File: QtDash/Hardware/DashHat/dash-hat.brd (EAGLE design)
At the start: 120.9 x 74.9 mm, 166 parts, among them IC1 LMV614, IC10 MAX9924, IC11 ZXTR2105FQ, IC2 MCP3X083008, IC3 MCP23017SS, IC4 LM358D, IC5 IL300, IC6 TSV912D, IC7 IL300, IC8 TSV912D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

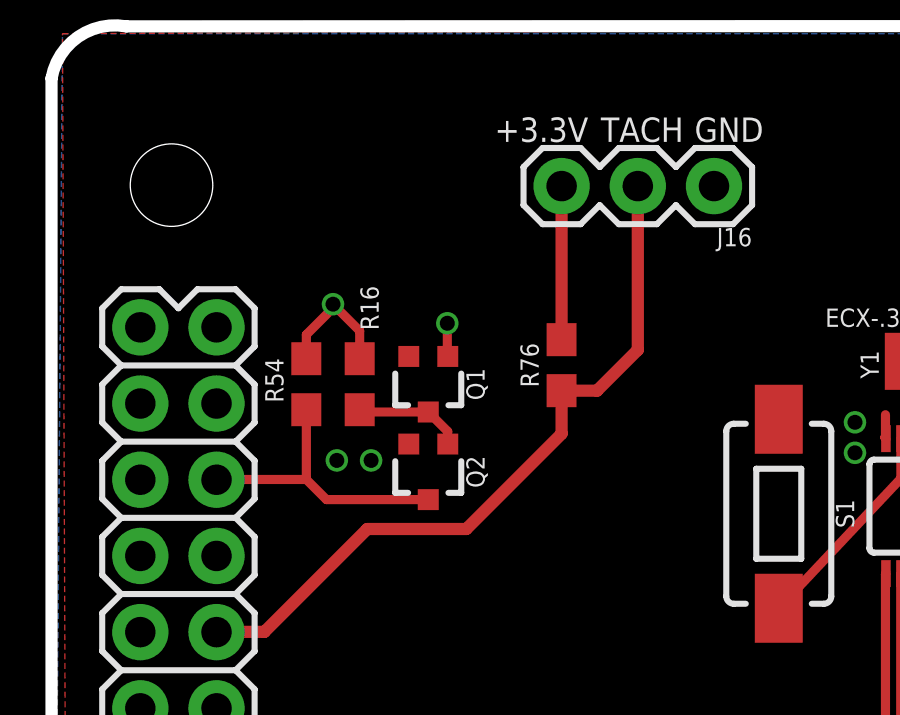
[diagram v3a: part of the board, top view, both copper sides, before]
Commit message: topic/hardware-revc: 	- reduced pullups directly on GPIOs from 1k to 20k 	- added pwm to rpi4 config and initial_turbo 	- slight layout changes
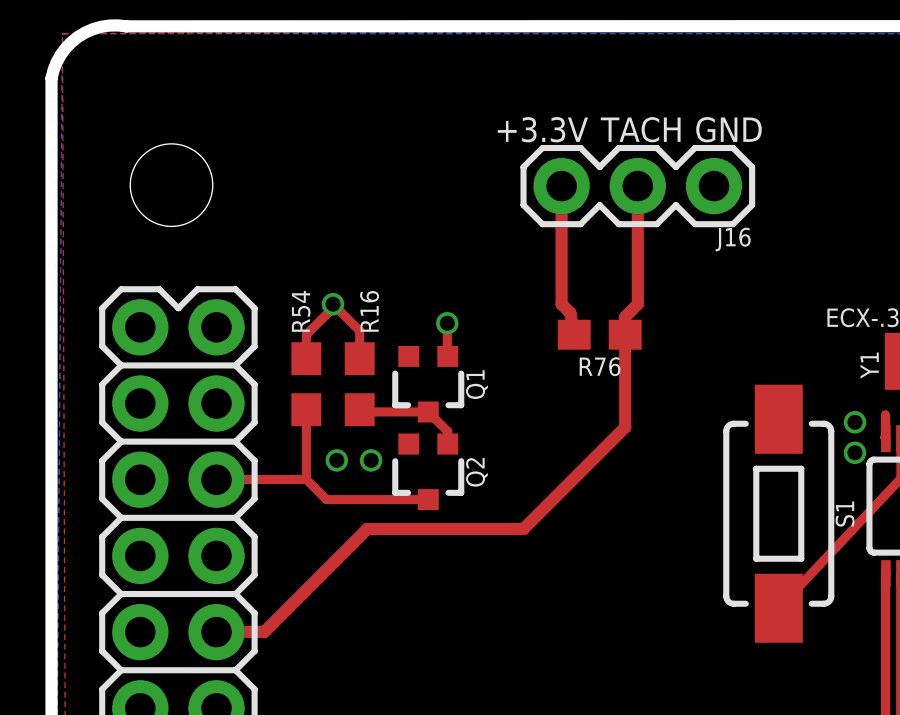
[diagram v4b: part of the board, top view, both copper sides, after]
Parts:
- R16, R54, R76: value 1k -> 20k
- moved R76 1.63 mm to (18.4, 56.5), turned to 180 degrees
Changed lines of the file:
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@@
 <layer number="25" name="tNames" color="58" fill="1" visible="yes" active="yes"/>
 <layer number="26" name="bNames" color="58" fill="1" visible="yes" active="yes"/>
-<layer number="27" name="tValues" color="7" fill="1" visible="yes" active="yes"/>
-<layer number="28" name="bValues" color="7" fill="1" visible="yes" active="yes"/>
+<layer number="27" name="tValues" color="7" fill="1" visible="no" active="yes"/>
+<layer number="28" name="bValues" color="7" fill="1" visible="no" active="yes"/>
 <layer number="29" name="tStop" color="7" fill="3" visible="yes" active="yes"/>
 <layer number="30" name="bStop" color="7" fill="6" visible="yes" active="yes"/>
@@
 <attribute name="PROD_ID" value="XXX-00000" x="22.225" y="61.468" size="1.778" layer="27" rot="R180" display="off"/>
 </element>
-<element name="R76" library="digital_dash" package="0603" value="1k" x="17.145" y="55.499" rot="R90"/>
+<element name="R76" library="digital_dash" package="0603" value="20k" x="18.415" y="56.515" rot="R180"/>
 <element name="R82" library="digital_dash" package="0617/17" value="RES_D+" x="109.474" y="47.879" smashed="yes" rot="R90">
 <attribute name="NAME" x="110.998" y="44.0436" size="1.27" layer="25" ratio="10" rot="R180"/>
@@
 <attribute name="VALUE" x="87.122" y="65.913" size="0.6096" layer="27" font="vector" ratio="20" rot="R90" align="top-center"/>
 </element>
-<element name="R16" library="digital_dash" package="0603" value="1k" x="10.414" y="54.864" smashed="yes" rot="R90">
-<attribute name="NAME" x="11.049" y="57.404" size="0.6096" layer="25" font="vector" ratio="20" rot="R90" align="bottom-center"/>
-<attribute name="VALUE" x="11.176" y="54.864" size="0.6096" layer="27" font="vector" ratio="20" rot="R90" align="top-center"/>
-</element>
-<element name="R54" library="digital_dash" package="0603" value="1k" x="8.636" y="54.864" smashed="yes" rot="R90">
-<attribute name="NAME" x="7.874" y="54.991" size="0.6096" layer="25" font="vector" ratio="20" rot="R90" align="bottom-center"/>
-<attribute name="VALUE" x="9.398" y="54.864" size="0.6096" layer="27" font="vector" ratio="20" rot="R90" align="top-center"/>
+<element name="R16" library="digital_dash" package="0603" value="20k" x="10.414" y="54.864" smashed="yes" rot="R90">
+<attribute name="NAME" x="11.049" y="57.277" size="0.6096" layer="25" font="vector" ratio="20" rot="R90" align="bottom-center"/>
+<attribute name="VALUE" value="20k" x="11.176" y="54.864" size="0.6096" layer="27" font="vector" ratio="20" rot="R90" align="top-center"/>
+</element>
+<element name="R54" library="digital_dash" package="0603" value="20k" x="8.636" y="54.864" smashed="yes" rot="R90">
+<attribute name="NAME" x="8.763" y="57.277" size="0.6096" layer="25" font="vector" ratio="20" rot="R90" align="bottom-center"/>
+<attribute name="VALUE" value="20k" x="9.398" y="54.864" size="0.6096" layer="27" font="vector" ratio="20" rot="R90" align="top-center"/>
 </element>
 <element name="J2" library="digital_dash" package="MOLEX-1053102108" value="CONN_04X2" x="25.908" y="4.953"/>
@@
 <wire x1="10.414" y1="55.714" x2="10.414" y2="56.642" width="0.3048" layer="1"/>
 <wire x1="10.414" y1="56.642" x2="9.525" y2="57.531" width="0.3048" layer="1"/>
-<wire x1="17.145" y1="61.468" x2="17.145" y2="56.349" width="0.4064" layer="1"/>
 <contactref element="R60" pad="2"/>
 <wire x1="15.367" y1="24.218" x2="15.367" y2="25.527" width="0.3048" layer="1"/>
@@
 <wire x1="42.164" y1="13.628" x2="43.395" y2="13.628" width="0.6096" layer="1"/>
 <wire x1="43.395" y1="13.628" x2="43.561" y2="13.462" width="0.6096" layer="1"/>
+<wire x1="17.145" y1="61.468" x2="17.184" y2="61.468" width="0.4064" layer="1"/>
+<wire x1="17.184" y1="61.468" x2="17.145" y2="61.429" width="0.4064" layer="1"/>
+<wire x1="17.145" y1="61.429" x2="17.145" y2="57.531" width="0.4064" layer="1"/>
+<wire x1="17.145" y1="57.531" x2="17.438" y2="57.238" width="0.4064" layer="1"/>
+<wire x1="17.438" y1="57.238" x2="17.565" y2="56.515" width="0.4064" layer="1"/>
 </signal>
 <signal name="!SPI_CS">
@@
 <contactref element="J16" pad="2"/>
 <contactref element="R76" pad="1"/>
-<wire x1="19.685" y1="61.468" x2="19.685" y2="56.007" width="0.4064" layer="1"/>
-<wire x1="19.685" y1="56.007" x2="18.327" y2="54.649" width="0.4064" layer="1"/>
-<wire x1="18.327" y1="54.649" x2="17.145" y2="54.649" width="0.4064" layer="1"/>
 <wire x1="5.642" y1="46.6" x2="5.651" y2="46.609" width="0.4064" layer="1"/>
 <wire x1="5.651" y1="46.609" x2="7.239" y2="46.609" width="0.4064" layer="1"/>
 <wire x1="7.239" y1="46.609" x2="10.668" y2="50.038" width="0.4064" layer="1"/>
-<wire x1="10.668" y1="50.038" x2="13.97" y2="50.038" width="0.4064" layer="1"/>
-<wire x1="13.97" y1="50.038" x2="17.145" y2="53.213" width="0.4064" layer="1"/>
-<wire x1="17.145" y1="53.213" x2="17.145" y2="54.649" width="0.4064" layer="1"/>
+<wire x1="10.668" y1="50.038" x2="15.875" y2="50.038" width="0.4064" layer="1"/>
+<wire x1="15.875" y1="50.038" x2="19.265" y2="53.428" width="0.4064" layer="1"/>
+<wire x1="19.685" y1="61.468" x2="19.685" y2="57.531" width="0.4064" layer="1"/>
+<wire x1="19.685" y1="57.531" x2="19.265" y2="57.111" width="0.4064" layer="1"/>
+<wire x1="19.265" y1="57.111" x2="19.265" y2="56.515" width="0.4064" layer="1"/>
+<wire x1="19.265" y1="53.428" x2="19.265" y2="56.515" width="0.4064" layer="1"/>
 </signal>
 <signal name="N$42">

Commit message: topic/hardware-revc: 	- added MCP2515 and SN65HVD230 to board 	- didn't use split termination or common mode choke for CAN -- if there is EMI issues that'll be one (of likely many) place to look
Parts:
- added C30, C31: 100n, digital_dash:0603
- added C32, C33: 22p, digital_dash:0603
- added D9: PESD1CAN, diode:SOT23
- added IC12: SN65HVD230D, digital_dash:SO08
- added J8: (no value), digital_dash:1X02
- added JP16: SPI_CS_SEL, SparkFun-Jumpers:SMT-JUMPER_3_NO_SILK
- added R77: 120 1%, digital_dash:0603
- added R80: 1k, digital_dash:0603
- added R81: 20k, digital_dash:0603
- added U1: MCP2515, SparkFun-IC-Comms:SO18W
- added X1: 12MHz, digital_dash:ECS
- moved S1 16.7 mm to (40.3, 45.2), flipped to the bottom, turned to 90 degrees
- moved R76 10.1 mm to (8.64, 59.1), flipped to the bottom, turned to 270 degrees
- moved IC9 8.99 mm to (36.2, 45.5), flipped to the bottom
- moved Y1 7.65 mm to (35.4, 50.5), flipped to the bottom
- moved J16 7.06 mm to (15.2, 62.5)
- moved C19 4.04 mm to (33.9, 44.3), flipped to the bottom, turned to 90 degrees
- moved R75 3.05 mm to (33.1, 41.8), flipped to the bottom, turned to 0 degrees
- moved C20 2.16 mm to (32.3, 44.3), flipped to the bottom, turned to 90 degrees
- moved JP22 1.78 mm to (10.2, 37.1), flipped to the bottom
- moved C8 1.28 mm to (21.7, 34.3)
- moved C7 1.28 mm to (23.2, 34.3)
- moved BT1 0.64 mm to (42.4, 55.2)
- moved Q2 0.28 mm to (12.6, 52.2), flipped to the bottom, turned to 270 degrees
- moved Q1 0.18 mm to (12.6, 55.0), flipped to the bottom, turned to 270 degrees
- moved R11 0.13 mm to (20.4, 11.2)
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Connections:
- new net !CAN_SPI_CS: JP16.2, U1.16
- new net CANH: D9.1, IC12.7, J8.1, R77.2
- new net CANL: D9.2, IC12.6, J8.2, R77.1
- new net GPIO25: J1.22, U1.12
- new net N$12: IC12.8, R80.1
- new net N$18: C32.2, U1.8, X1.1
- new net N$31: C33.1, U1.7, X1.2
- new net N$37: IC12.4, U1.2
- new net N$40: IC12.1, U1.1
- new net N$43: R81.1, U1.17
- net 3.3V: now also C30.1, C31.1, IC12.3, R81.2, U1.18
- net GND: now also C30.2, C31.2, C32.1, C33.2, D9.3, IC12.2, R80.2, U1.9
- net SPI_CE0_N: now also JP16.3
- net SPI_CE1_N: now also JP16.1
- net SPI_CLK: now also U1.13
- net SPI_MISO: now also U1.15
- net SPI_MOSI: now also U1.14
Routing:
- net GPIO25: track 0.00 -> 28.0 mm, vias 0 -> 1
- net !CAN_SPI_CS: track 0.00 -> 20.3 mm, vias 0 -> 1
- net CANH: track 0.00 -> 18.5 mm
- net SPI_MISO: track 27.5 -> 39.0 mm, vias 0 -> 2
- net SPI_MOSI: track 28.0 -> 38.7 mm
- net N$37: track 0.00 -> 10.6 mm
- net SCL: track 81.9 -> 71.9 mm, vias 2 -> 1
- net SDA: track 85.1 -> 75.7 mm, vias 2 -> 3
- net CANL: track 0.00 -> 8.97 mm
- net SPI_CE0_N: track 7.72 -> 16.6 mm, vias 0 -> 1
- net SPI_CLK: track 27.1 -> 35.5 mm
- net N$18: track 0.00 -> 8.15 mm
- net N$31: track 0.00 -> 8.04 mm
- net N$39: track 10.0 -> 2.90 mm
- net 3.3V: track 81.4 -> 88.2 mm, vias 11 -> 13
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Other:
- board text added: "Volvo 240 Pi Dash Adapter Rev C. May 2022 @whitfijs"
- board text removed: "Volvo 240 Pi Dash Adapter Rev C. Apr 2022 @whitfijs"

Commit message: topic/hardware-revc: 	- added parts list for rev c
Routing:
- net N$18: track 8.15 -> 7.35 mm
- net N$31: track 8.04 -> 8.68 mm

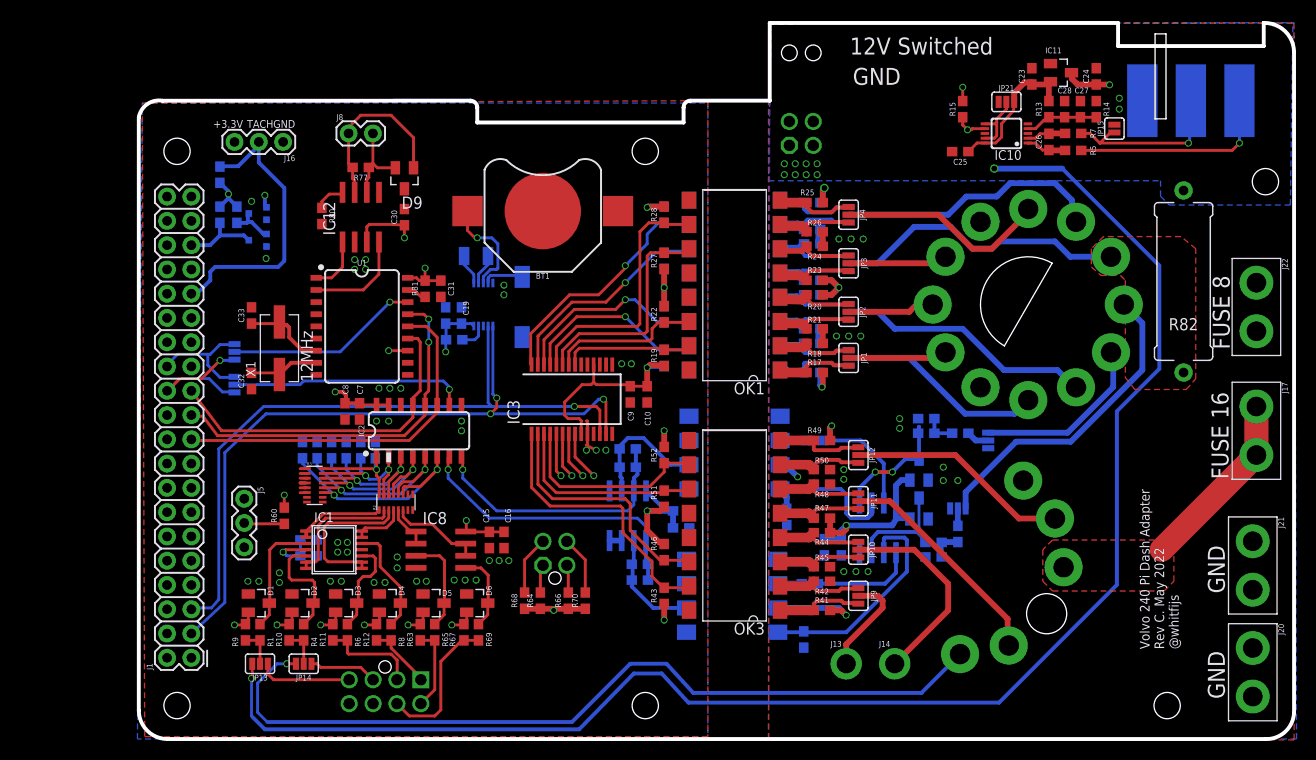
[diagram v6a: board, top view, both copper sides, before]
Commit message: topic/hardware-revc: 	- fixed (hopefully) some string comparision issues in sensor utils and config 	- updated mcp2515 and transceiver circuit -- todo: check dimensions of cheap amazon JST style plug
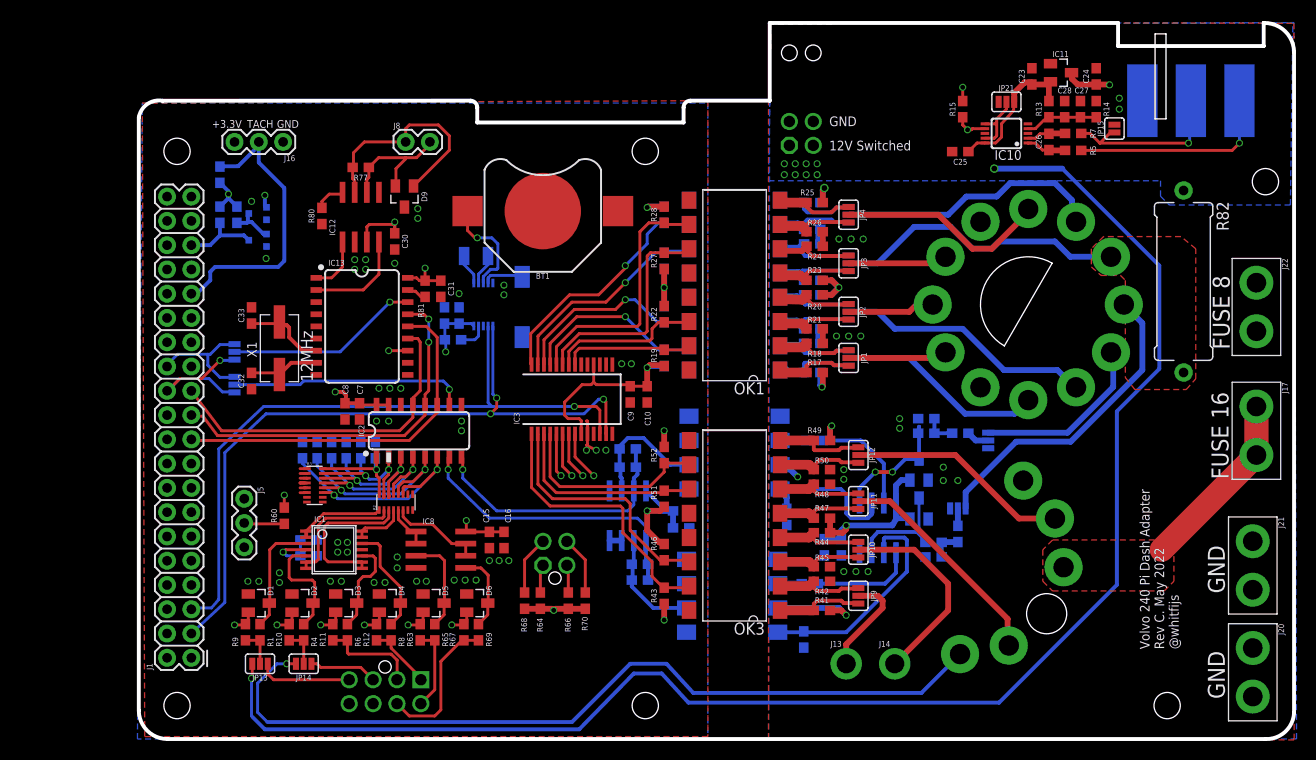
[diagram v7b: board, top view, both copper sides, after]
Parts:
- moved J8 6.03 mm to (28.1, 62.5)
- moved C30 2.74 mm to (26.9, 52.1), turned to 270 degrees
- moved D9 1.91 mm to (27.9, 56.8)
- moved C19 0.25 mm to (33.7, 44.3)
- moved C20 0.13 mm to (32.1, 44.3)
- moved R75 0.13 mm to (33.0, 41.8)
- renumbered U1 to IC13
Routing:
- net CANH: track 18.5 -> 23.6 mm
- net CANL: track 8.97 -> 13.7 mm
- net AC_RELAY/VSS_TO_ECU: track 114.3 -> 115.2 mm
- net GND: vias 42 -> 46
